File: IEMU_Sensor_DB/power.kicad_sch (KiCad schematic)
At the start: 56 parts, among them J101 USB4125-GF-A, J102 DF13-4P-1.25H_51_, Q101 CSD85301Q2, U101 NPM1304-QEAA-R7, U102 BQ29702DSER, U103 TLV75530PDRVR, U104 INA216A2RSWR

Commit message: implemented changes from the review with TF and fixed lost parts in the library
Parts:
- renumbered TP101 to TP102
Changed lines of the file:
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@@
 		(on_board yes)
 		(dnp no)
-		(property "Reference" "TP101"
+		(property "Reference" "TP102"
 			(at 88.646 81.026 0)
 			(effects
@@
 			(project "IEMU"
 				(path "/114b31f2-6a4f-42ef-aa97-5a200e091126/ecb55954-6122-4552-9eac-22683e31d0d4"
-					(reference "TP101")
+					(reference "TP102")
 					(unit 1)
 				)

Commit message: finished schematic revision based on TF-review by implementing sensor schematic too
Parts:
- removed D101, D102: TPD1E10B06DYAR, Diode_SMD:D_SOD-523, symbol 0_Power:TPD1E10B06DYAR
- removed D103, D104: RCLAMP3321P-N, Diode_SMD:D_SOD-882, symbol 0_Connectors:RCLAMP3321P-N
- removed J101: USB4125-GF-A, 0_Connectors:GCT_USB4125-GF-A_REVA2, symbol 0_Connectors:USB4125-GF-A
- removed J102: DF13-4P-1.25H_51_, 0_Connectors:HRS_DF13-4P-1.25H_75_, symbol 0_Connectors:DF13-4P-1.25H_75_
- added D101, D102, D103, D106, D110: ESD5Z5.0T1G, Diode_SMD:D_SOD-523_1, symbol 0_Power:ESD5Z5.0T1G
- added D107, D108: ESD9L1P8, Diode_SMD:D_SOD-882, symbol 0_Power:ESD9L1P8
- added D111: TPD1E10B06DYAR, Diode_SMD:D_SOD-523, symbol 0_Power:TPD1E10B06DYAR
- added J101: USB4125-GF-A, 0_Connectors:GCT_USB4125-GF-A_REVA2, symbol 0_Connectors:USB4125-GF-A_REVA2
- added J102: DF13-4P-1.25H(21), 0_Connectors:DF13-4P-1.25H(21), symbol 0_Connectors:DF13-4P-1.25H(21)
- D109: renamed from D105; Distributer Link 1 https://www.mouser.de/ProductDetail/LITEON/LTST-C19HE1WT?qs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 -> (none); Distributor Link 1 (none) -> https://www.mouser.de/ProductDetail/LITEON/LTST-C19HE1WT?qs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
- renumbered D106 to D104, D107 to D105
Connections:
- net +VBAT: now also D110.1 (I/O)
- net +VBUS_IN_CONN: now also D106.1 (I/O), J102.1
- net +VBUS_IN_USB: now also D101.1 (I/O), J101.A9 (VBUS), J101.B9 (VBUS)
- net BAT-: now also D111.1 (I/O)
- net CC1: now also D102.1 (I/O), J101.A5 (CC1)
- net CC2: now also D103.1 (I/O), J101.B5 (CC2)
- net GND: now also D101.2 (GND), D102.2 (GND), D103.2 (GND), D106.2 (GND), D107.2 (GND), D108.2 (GND), D110.2 (GND), D111.2 (GND), J101.A12 (GND), J101.B12 (GND), J101.S1 (SHIELD), J101.S2 (SHIELD), J101.S3 (SHIELD), J101.S4 (SHIELD), J102.2
- net at R101.1, R110.1, TP110.1: now also D108.1 (I/O), J102.3
- net at R109.1, TP111.1: now also D107.1 (I/O), J102.4

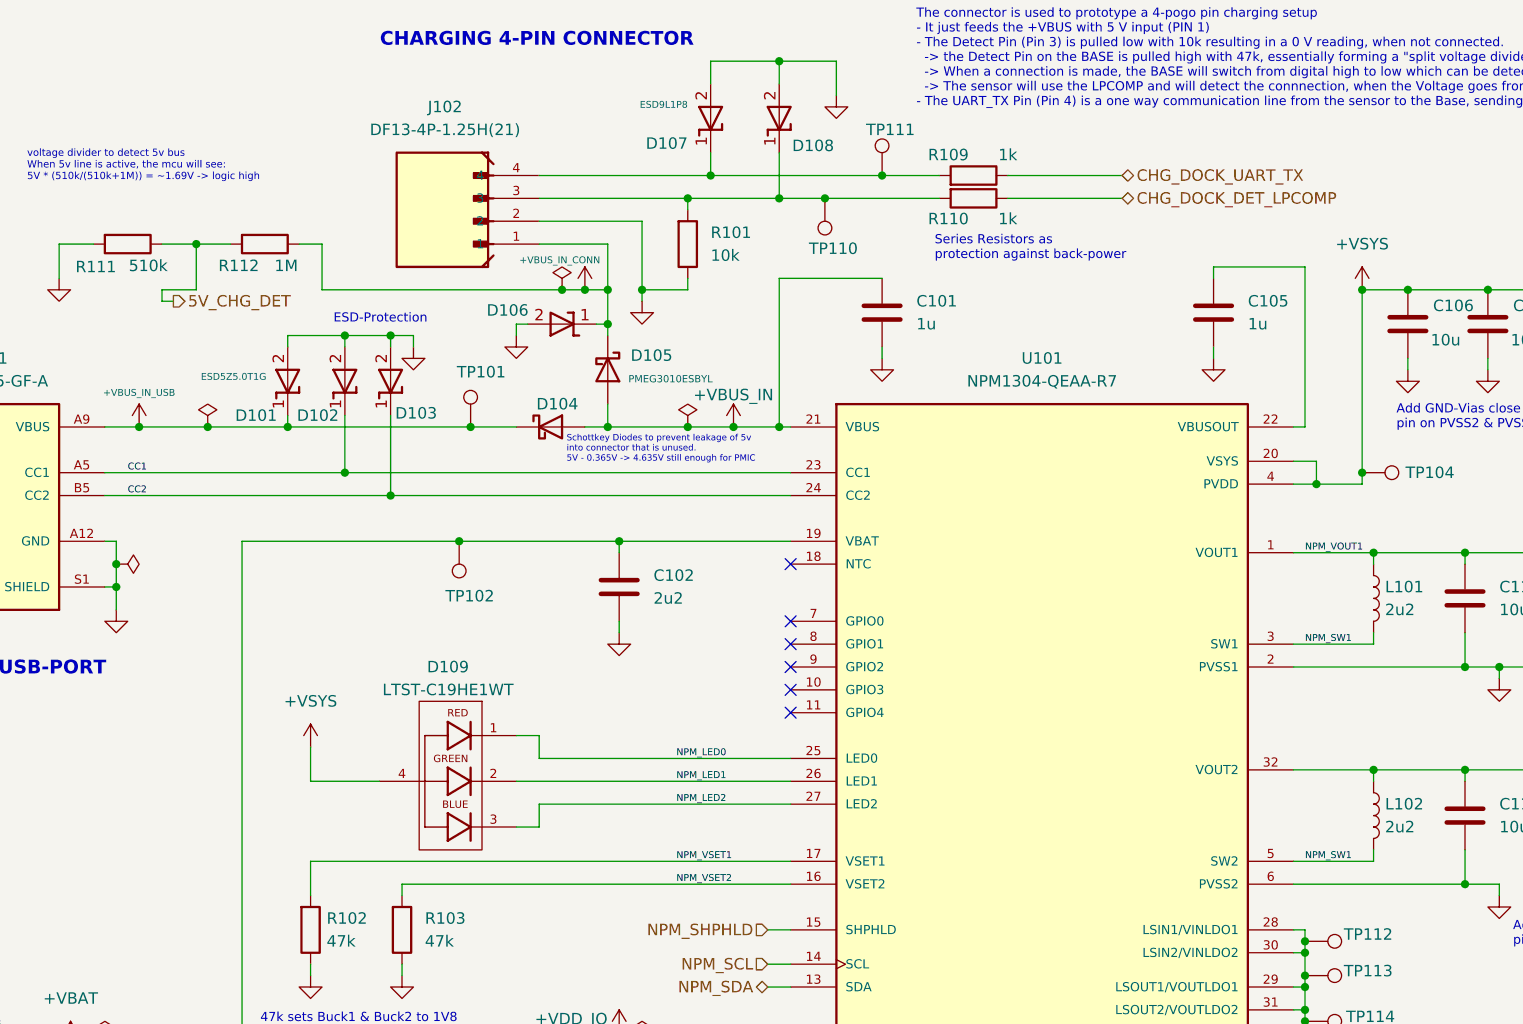
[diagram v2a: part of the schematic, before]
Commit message: created the layout for the sensor (not finished)
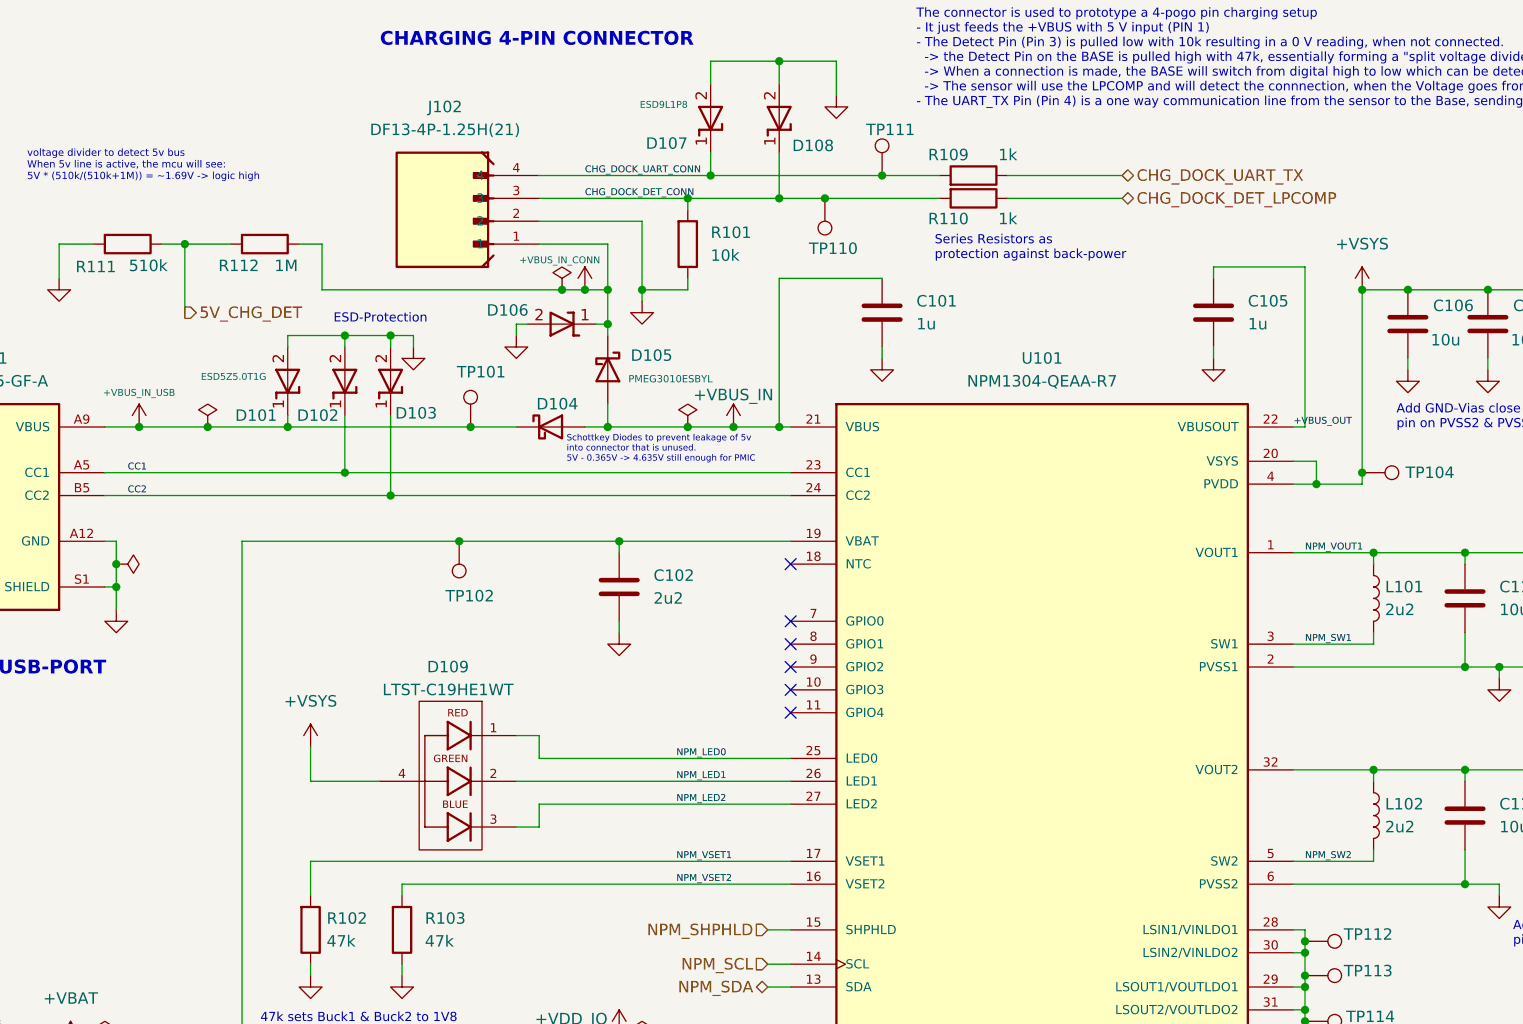
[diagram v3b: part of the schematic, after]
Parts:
- TP101, TP102, TP103, TP104, TP105, TP106, TP107, TP108, TP109, TP110, TP111, TP112, TP113, TP114: footprint TestPoint:TestPoint_Pad_D2.0mm -> TestPoint:TestPoint_Pad_D1.0mm
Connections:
- net GND: now also U103.7 (GND)
- net NPM_SW1: no longer L102.2, U101.5 (SW2)
- net CHG_DOCK_UART_CONN: now reaches D107.1 (I/O), J102.4, R109.1, TP111.1
- net CHG_DOCK_DET_CONN: now reaches D108.1 (I/O), J102.3, R101.1, R110.1, TP110.1
- net +VBUS_OUT: now reaches C105.1, U101.22 (VBUSOUT)
- new net NC: U102.1 (NC)
- new net NPM_SW2: L102.2, U101.5 (SW2)
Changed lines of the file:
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@@
 	)
 	(junction
+		(at 59.69 41.91)
+		(diameter 0)
+		(color 0 0 0 0)
+	)
+	(junction
 		(at 86.36 182.88)
 		(diameter 0)
@@
 	)
 	(junction
-		(at 60.96 41.91)
-		(diameter 0)
-		(color 0 0 0 0)
-	)
-	(junction
 		(at 252.73 76.2)
 		(diameter 0)
@@
 	(wire
 		(pts
-			(xy 57.15 41.91) (xy 60.96 41.91)
+			(xy 57.15 41.91) (xy 59.69 41.91)
 		)
 		(stroke
@@
 	(wire
 		(pts
-			(xy 57.15 48.26) (xy 58.42 48.26)
-		)
-		(stroke
-			(width 0)
-			(type default)
-		)
-	)
-	(wire
-		(pts
 			(xy 50.8 69.85) (xy 82.55 69.85)
 		)
@@
 	(wire
 		(pts
-			(xy 60.96 41.91) (xy 64.77 41.91)
-		)
-		(stroke
-			(width 0)
-			(type default)
-		)
-	)
-	(wire
-		(pts
 			(xy 184.15 120.65) (xy 184.15 123.19)
 		)
@@
 	(wire
 		(pts
-			(xy 57.15 46.99) (xy 57.15 48.26)
-		)
-		(stroke
-			(width 0)
-			(type default)
-		)
-	)
-	(wire
-		(pts
 			(xy 246.38 83.82) (xy 246.38 76.2)
 		)
@@
 	(wire
 		(pts
-			(xy 60.96 41.91) (xy 60.96 46.99)
-		)
-		(stroke
-			(width 0)
-			(type default)
-		)
-	)
-	(wire
-		(pts
 			(xy 237.49 60.96) (xy 237.49 64.77)
 		)
@@
 	(wire
 		(pts
+			(xy 59.69 41.91) (xy 59.69 49.53)
+		)
+		(stroke
+			(width 0)
+			(type default)
+		)
+	)
+	(wire
+		(pts
 			(xy 68.58 156.21) (xy 73.66 156.21)
 		)
@@
 	(wire
 		(pts
+			(xy 59.69 41.91) (xy 64.77 41.91)
+		)
+		(stroke
+			(width 0)
+			(type default)
+		)
+	)
+	(wire
+		(pts
 			(xy 86.36 182.88) (xy 81.28 182.88)
 		)
@@
 	(wire
 		(pts
-			(xy 60.96 46.99) (xy 57.15 46.99)
-		)
-		(stroke
-			(width 0)
-			(type default)
-		)
-	)
-	(wire
-		(pts
 			(xy 83.82 113.03) (xy 127 113.03)
 		)
@@
 		)
 	)
-	(label "NPM_SW1"
+	(label "NPM_SW2"
 		(at 184.15 110.49 0)
 		(effects
@@
 		)
 	)
+	(label "+VBUS_OUT"
+		(at 182.88 62.23 0)
+		(effects
+			(font
+				(size 0.762 0.762)
+			)
+			(justify left bottom)
+		)
+	)
 	(label "NPM_LED2"
 		(at 114.3 104.14 0)
@@
 		)
 	)
+	(label "CHG_DOCK_DET_CONN"
+		(at 104.14 36.83 0)
+		(effects
+			(font
+				(size 0.762 0.762)
+			)
+			(justify left bottom)
+		)
+	)
+	(label "CHG_DOCK_UART_CONN"
+		(at 104.14 34.29 0)
+		(effects
+			(font
+				(size 0.762 0.762)
+			)
+			(justify left bottom)
+		)
+	)
 	(label "BAT_P_COUT"
 		(at 74.93 147.32 0)
@@
 	(hierarchical_label "5V_CHG_DET"
 		(shape output)
-		(at 58.42 48.26 0)
+		(at 59.69 49.53 0)
 		(effects
 			(font
@@
 			)
 		)
-		(property "Footprint" "TestPoint:TestPoint_Pad_D2.0mm"
+		(property "Footprint" "TestPoint:TestPoint_Pad_D1.0mm"
 			(at 237.49 66.04 0)
 			(effects
@@
 			)
 		)
-		(property "Footprint" "TestPoint:TestPoint_Pad_D2.0mm"
+		(property "Footprint" "TestPoint:TestPoint_Pad_D1.0mm"
 			(at 62.23 170.18 0)
 			(effects
@@
 			)
 		)
-		(property "Footprint" "TestPoint:TestPoint_Pad_D2.0mm"
+		(property "Footprint" "TestPoint:TestPoint_Pad_D1.0mm"
 			(at 184.15 128.27 0)
 			(effects
@@
 			)
 		)
-		(property "Footprint" "TestPoint:TestPoint_Pad_D2.0mm"
+		(property "Footprint" "TestPoint:TestPoint_Pad_D1.0mm"
 			(at 250.19 100.33 0)
 			(effects
@@
 			)
 		)
-		(property "Footprint" "TestPoint:TestPoint_Pad_D2.0mm"
+		(property "Footprint" "TestPoint:TestPoint_Pad_D1.0mm"
 			(at 184.15 124.46 0)
 			(effects
@@
 			)
 		)
-		(property "Footprint" "TestPoint:TestPoint_Pad_D2.0mm"
+		(property "Footprint" "TestPoint:TestPoint_Pad_D1.0mm"
 			(at 273.05 46.99 0)
 			(effects
@@
 			)
 		)
-		(property "Footprint" "TestPoint:TestPoint_Pad_D2.0mm"
+		(property "Footprint" "TestPoint:TestPoint_Pad_D1.0mm"
 			(at 95.25 74.93 0)
 			(effects
@@
 			)
 		)
-		(property "Footprint" "TestPoint:TestPoint_Pad_D2.0mm"
+		(property "Footprint" "TestPoint:TestPoint_Pad_D1.0mm"
 			(at 257.81 88.9 0)
 			(effects
@@
 			)
 		)
-		(property "Footprint" "TestPoint:TestPoint_Pad_D2.0mm"
+		(property "Footprint" "TestPoint:TestPoint_Pad_D1.0mm"
 			(at 142.24 34.29 0)
 			(effects
@@
 			)
 		)
-		(property "Distributer Link 1" ""
-			(at 59.69 153.67 0)
-			(effects
-				(font
-					(size 1.27 1.27)
-				)
-				(hide yes)
-			)
-		)
-		(property "Manufactuer_Name" ""
-			(at 59.69 153.67 0)
-			(effects
-				(font
-					(size 1.27 1.27)
-				)
-				(hide yes)
-			)
-		)
 		(pin "4"
 		)
@@
 		(pin "5"
 		)
+		(pin "1"
+		)
 		(instances
 			(project ""
@@
 			)
 		)
-		(property "Footprint" "TestPoint:TestPoint_Pad_D2.0mm"
+		(property "Footprint" "TestPoint:TestPoint_Pad_D1.0mm"
 			(at 96.52 62.23 0)
 			(effects
@@
 			)
 		)
-		(property "Distributer Link 1" ""
-			(at 237.49 46.99 0)
-			(effects
-				(font
-					(size 1.27 1.27)
-				)
-				(hide yes)
-			)
-		)
-		(property "Manufactuer_Name" ""
-			(at 237.49 46.99 0)
-			(effects
-				(font
-					(size 1.27 1.27)
-				)
-				(hide yes)
-			)
-		)
 		(pin "5"
 		)
@@
 		(pin "4"
 		)
+		(pin "7"
+		)
 		(instances
 			(project ""
@@
 			)
 		)
-		(property "Footprint" "TestPoint:TestPoint_Pad_D2.0mm"
+		(property "Footprint" "TestPoint:TestPoint_Pad_D1.0mm"
 			(at 184.15 133.35 0)
 			(effects
@@
 			)
 		)
-		(property "Footprint" "TestPoint:TestPoint_Pad_D2.0mm"
+		(property "Footprint" "TestPoint:TestPoint_Pad_D1.0mm"
 			(at 190.5 62.23 0)
 			(effects
@@
 			)
 		)
-		(property "Footprint" "TestPoint:TestPoint_Pad_D2.0mm"
+		(property "Footprint" "TestPoint:TestPoint_Pad_D1.0mm"
 			(at 254 76.2 0)
 			(effects
@@
 			)
 		)
-		(property "Footprint" "TestPoint:TestPoint_Pad_D2.0mm"
+		(property "Footprint" "TestPoint:TestPoint_Pad_D1.0mm"
 			(at 135.89 36.83 0)
 			(effects

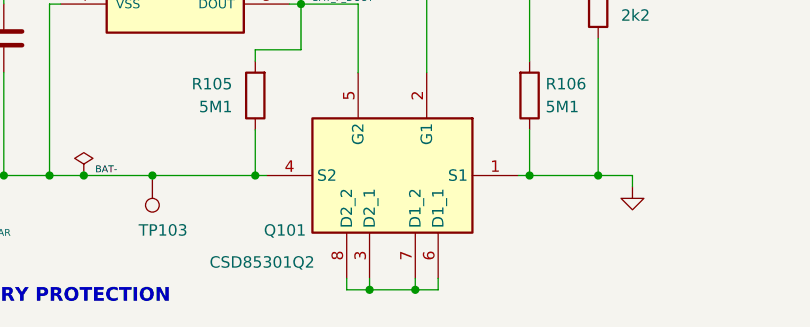
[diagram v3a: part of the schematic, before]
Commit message: finished layout for sensor
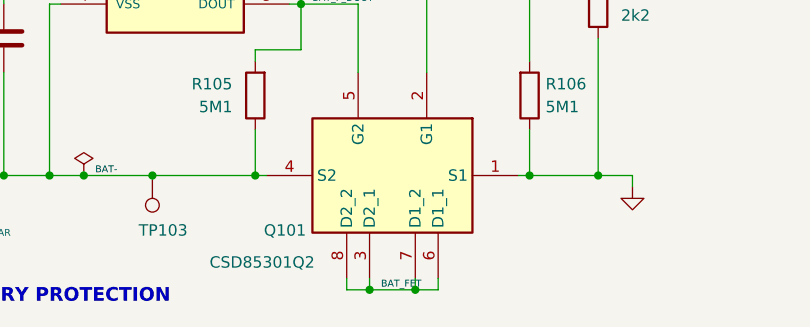
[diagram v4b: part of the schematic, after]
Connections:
- net BAT_FET: now reaches Q101.3 (D2_1), Q101.6 (D1_1), Q101.7 (D1_2), Q101.8 (D2_2)
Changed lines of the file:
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@@
+		)
+	)
+	(label "BAT_FET"
+		(at 82.55 182.88 0)
+		(effects
+			(font
+				(size 0.762 0.762)
+			)
+			(justify left bottom)
 		)
 	)
